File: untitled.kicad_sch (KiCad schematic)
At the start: 88 parts, among them J4 MX-NoLED, K1 MX-NoLED, M1 MX-NoLED, P1 MX-NoLED, Q1 MX-NoLED, T1 MX-NoLED, U4 MX-NoLED, X1 MX-NoLED, Y2 MX-NoLED

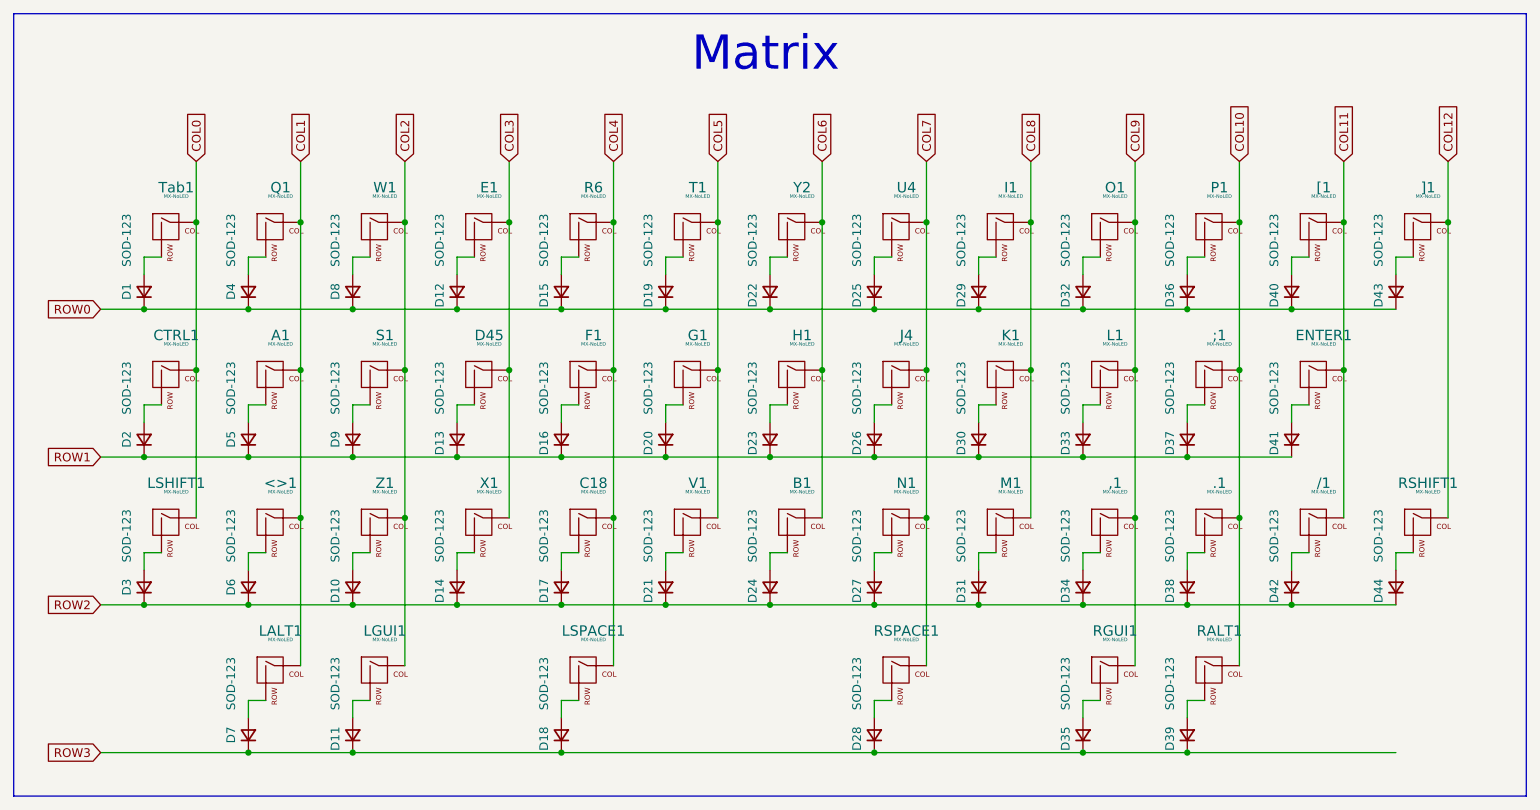
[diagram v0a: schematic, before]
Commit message: add qspi_ss pullup
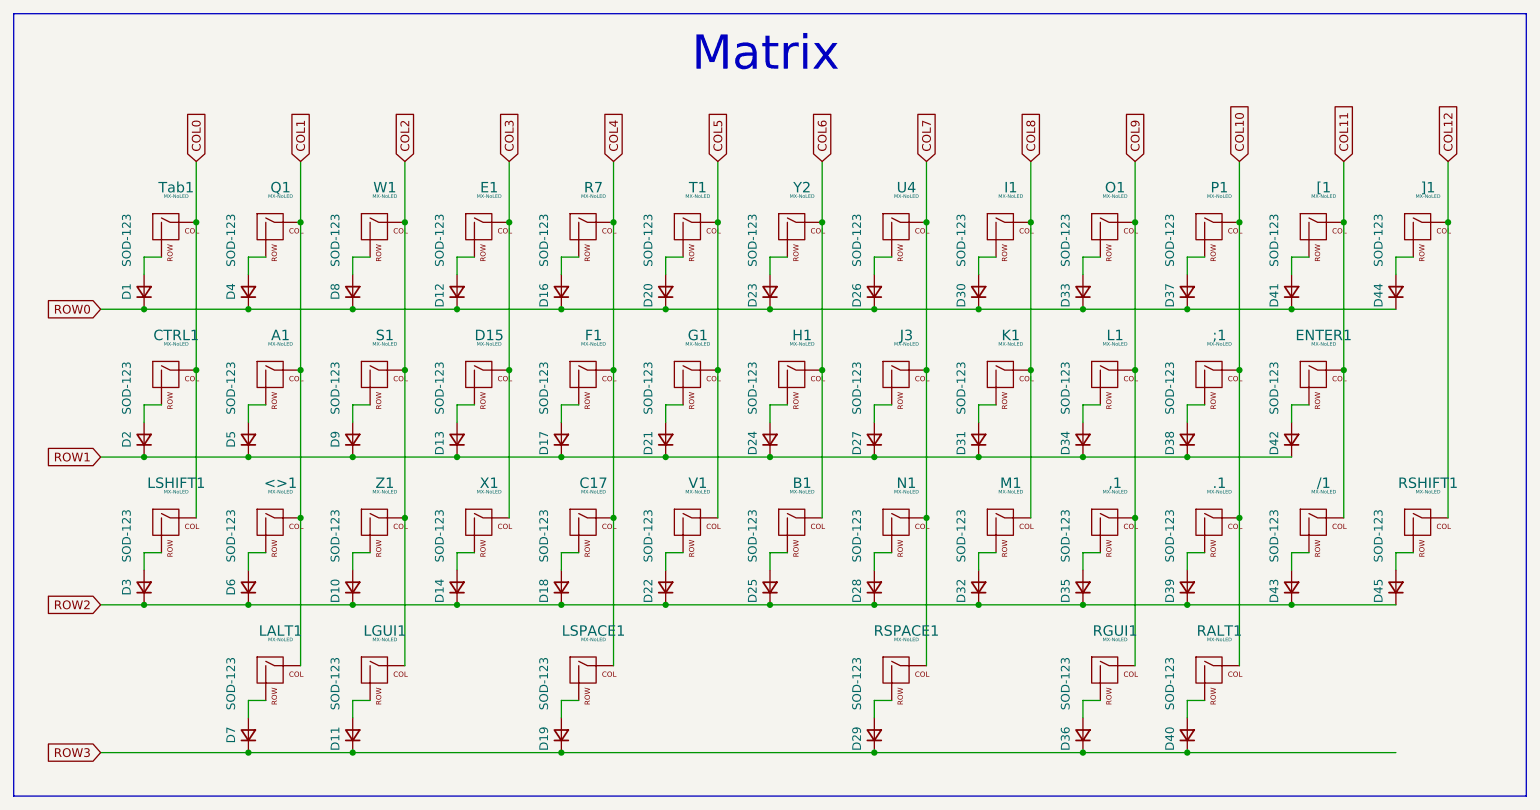
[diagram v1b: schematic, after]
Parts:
- renumbered C18 to C17, D45 to D15, D15 to D16, D16 to D17, D17 to D18, D18 to D19, D19 to D20, D20 to D21, D21 to D22, D22 to D23, D23 to D24, D24 to D25, D25 to D26, D26 to D27, D27 to D28, D28 to D29, D29 to D30, D30 to D31, D31 to D32, D32 to D33, D33 to D34, D34 to D35, D35 to D36, D36 to D37, D37 to D38, D38 to D39, D39 to D40, D40 to D41, D41 to D42, D42 to D43, D43 to D44, D44 to D45, J4 to J3, R6 to R7
